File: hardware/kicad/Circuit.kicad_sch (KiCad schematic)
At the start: 46 parts, among them J1 USB_C_Receptacle_USB2.0_14P, J2 B2B-XH-A__LF__SN_, Q1 AO3401A, Q2 AO3401A, U1 BQ24075RGT, U2 TPS63070RNMR

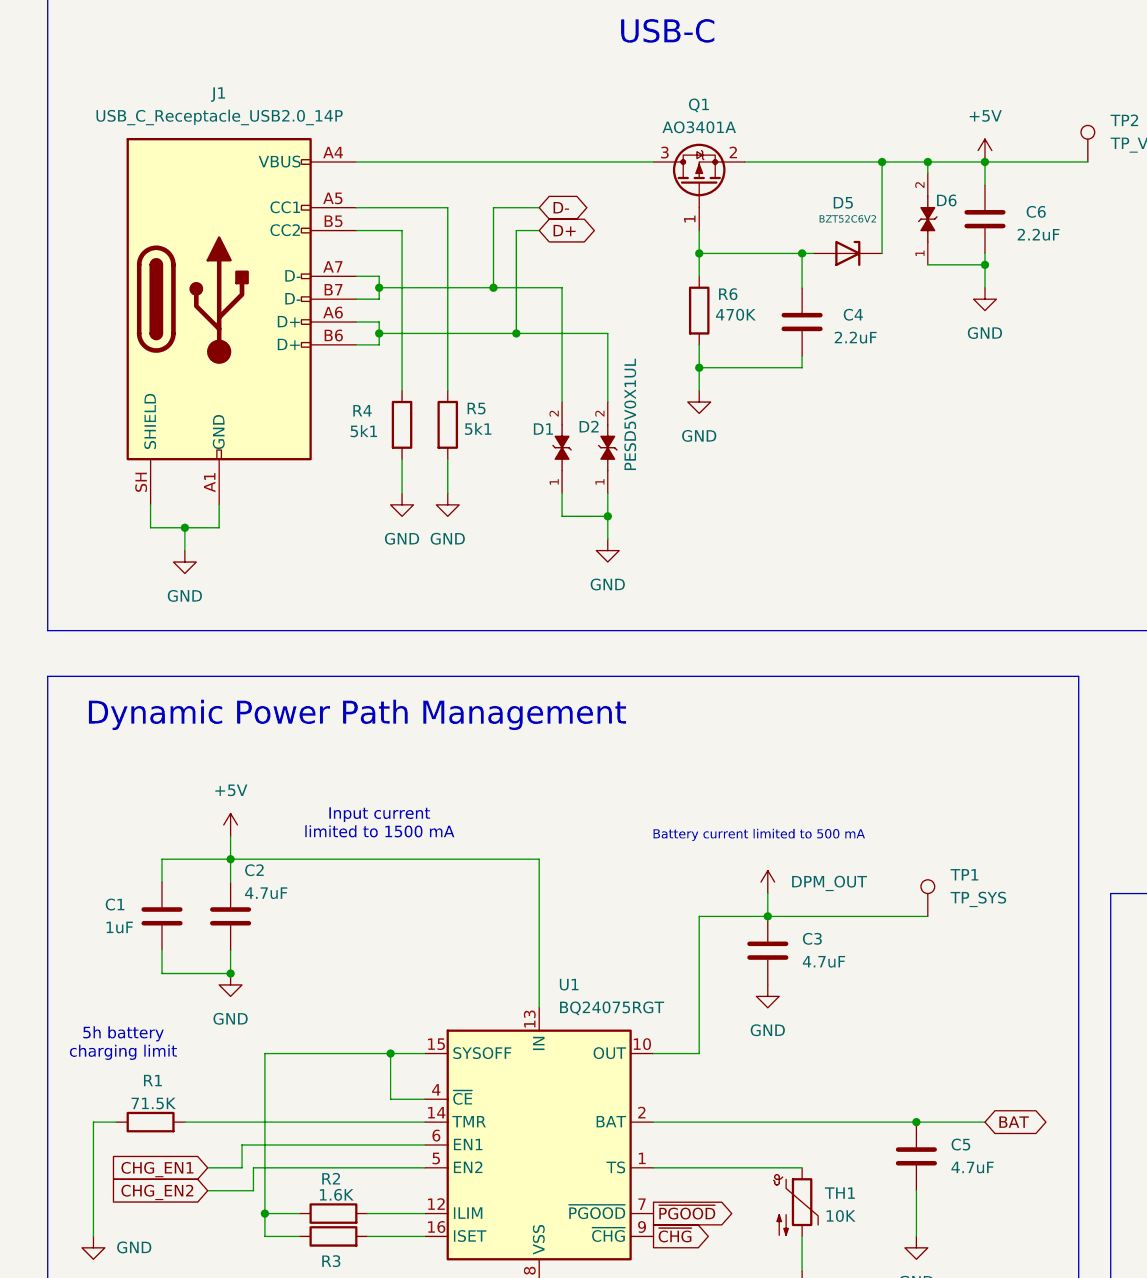
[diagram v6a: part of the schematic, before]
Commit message: feat: manufacturer part numbers
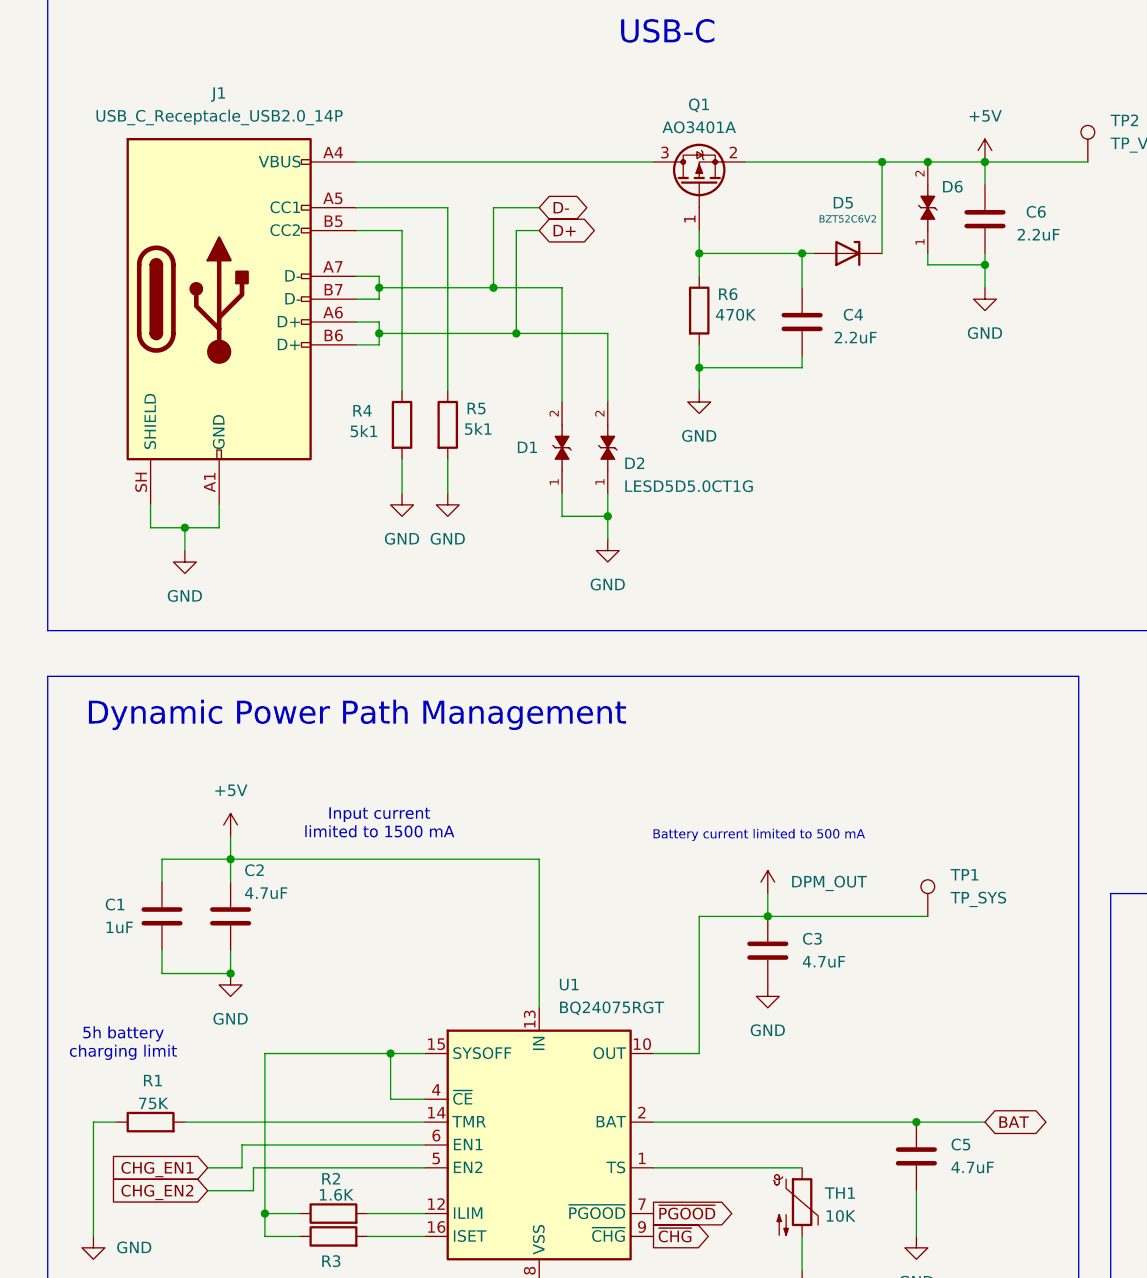
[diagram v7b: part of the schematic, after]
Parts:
- C1: LCSC (none) -> C59782
- C10: LCSC (none) -> C92806
- C11, C13: LCSC (none) -> C1590
- C12: LCSC (none) -> C86295
- C2, C3, C5: LCSC (none) -> C108342
- C4, C6: LCSC (none) -> C43922
- C7, C8, C9: LCSC (none) -> C237435
- D1, D2: value PESD5V0X1UL -> LESD5D5.0CT1G; LCSC (none) -> C5246195
- D6: value ESD5Z6.8T1G -> LESD5D5.0CT1G; LCSC (none) -> C5246195
- J1: LCSC (none) -> C165948
- J2: LCSC (none) -> C158012
- L1: footprint Inductor_SMD:L_0603_1608Metric -> AOTA-B252010S1R5MT:INDC2520X100N; LCSC (none) -> C24383011
- Q1, Q2: LCSC (none) -> C15127
- R1: value 71.5K -> 75K; LCSC (none) -> C18671
- R10, R11, R12, R16, R9: LCSC (none) -> C15458
- R13: LCSC (none) -> C15401
- R14: LCSC (none) -> C23178
- R15: LCSC (none) -> C22807
- R2: LCSC (none) -> C22847
- R3: LCSC (none) -> C13118
- R4, R5: LCSC (none) -> C14677
- R6: LCSC (none) -> C25599
- R7, R8: LCSC (none) -> C25989
- TH1: footprint Resistor_SMD:R_0603_1608Metric -> PCM_JLCPCB:R_0603; LCSC (none) -> C525660
- U1: LCSC (none) -> C15464
- U2: LCSC (none) -> C109322
